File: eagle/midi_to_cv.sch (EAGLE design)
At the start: 49 parts, among them IC1 TL084P, IC2 TL084P, U1 ATMEGA328P_PDIP

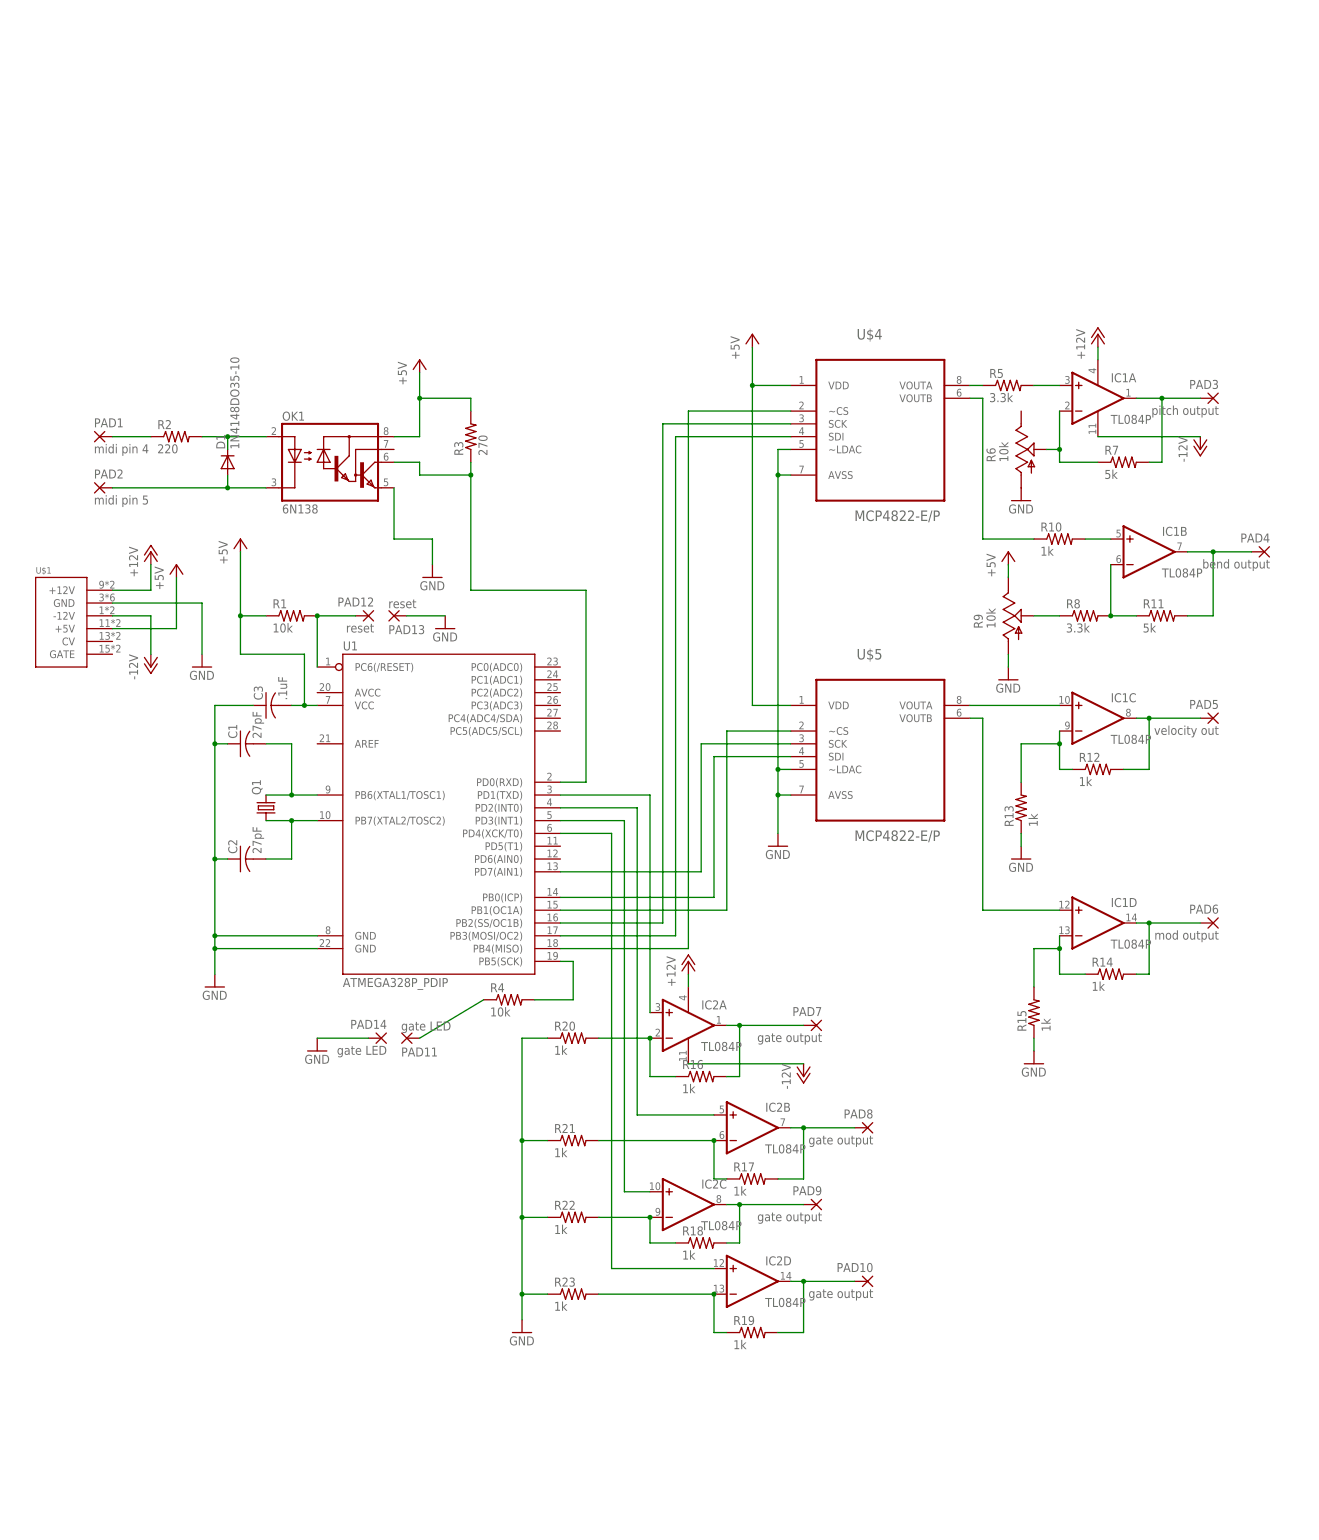
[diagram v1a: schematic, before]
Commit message: this interface is getting sirius
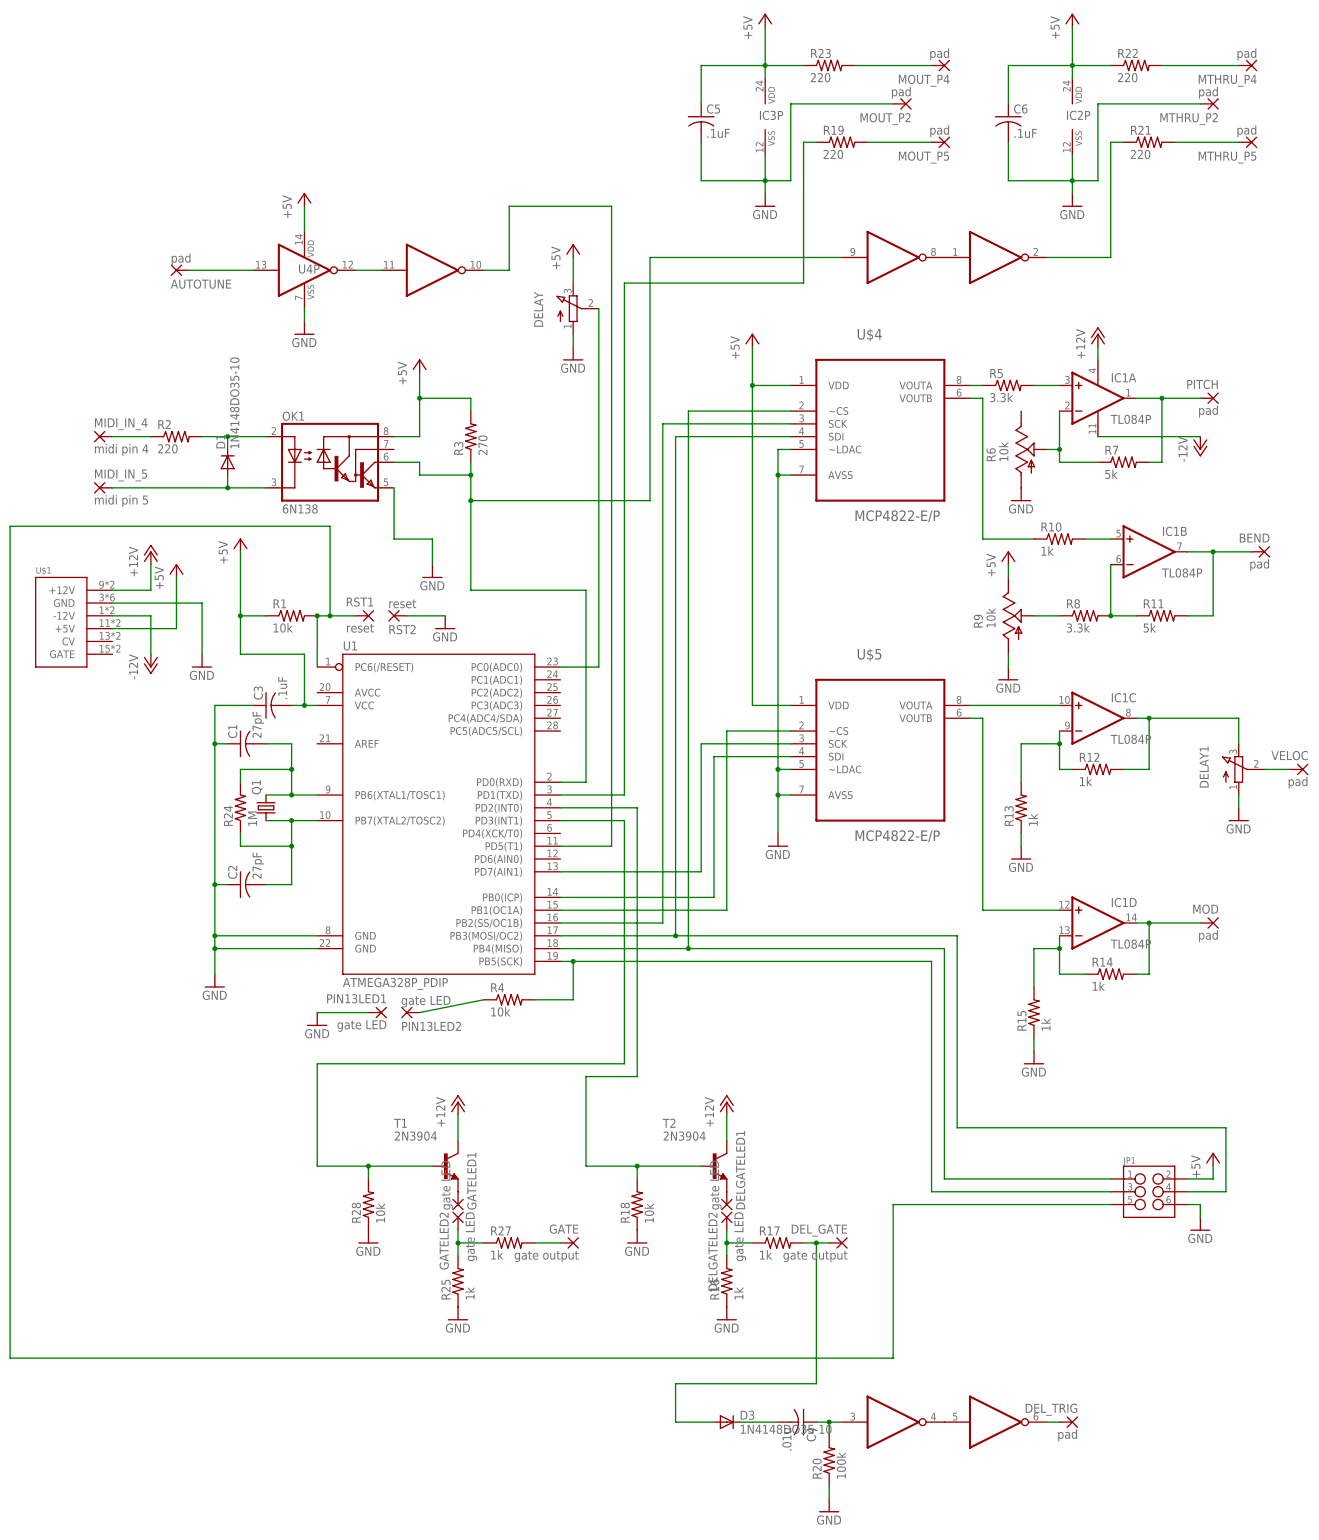
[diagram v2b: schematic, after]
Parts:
- removed PAD10, PAD7, PAD8, PAD9: gate output, wirepad:2,54/0,9
- removed PAD11, PAD14: gate LED, wirepad:2,54/0,9
- removed PAD5: velocity out, wirepad:2,54/0,9
- added AUTOTUNE, DEL_TRIG, MOUT_P2, MOUT_P4, MOUT_P5, MTHRU_P2, MTHRU_P4, MTHRU_P5, VELOC: pad, wirepad:2,54/0,9
- added C4: .01u, rcl:C-US050-024X044
- added C5, C6: .1uF, rcl:C-US025-040X050
- added D3: 1N4148DO35-10, diode:1N4148DO35-10
- added DELAY, DELAY1: (no value), pot:3RP/1610N
- added DELGATELED1, DELGATELED2, GATELED1, GATELED2, PIN13LED1, PIN13LED2: gate LED, wirepad:2,54/0,9
- added DEL_GATE, GATE: gate output, wirepad:2,54/0,9
- added IC3: 4067N, 40xx:4067N
- added JP1: (no value), SparkFun-Connectors:M03X2NO_SILK
- added R24: 1M, rcl:R-US_0207/10
- added R25, R27: 1k, rcl:R-US_0207/10
- added R28: 10k, rcl:R-US_0207/10
- added T1, T2: 2N3904, transistor:2N3904
- added U4: 4584N, TR808clone:4584N
- BEND: value bend output -> pad
- IC2: value TL084P -> 4067N; device linear:TL084P -> 40xx:4067N
- MOD: value mod output -> pad
- PITCH: value pitch output -> pad
- R18: value 1k -> 10k
- R19, R21, R22, R23: value 1k -> 220
- R20: value 1k -> 100k
- renumbered PAD1 to MIDI_IN_4, PAD12 to RST1, PAD13 to RST2, PAD2 to MIDI_IN_5, PAD3 to PITCH, PAD4 to BEND, PAD6 to MOD
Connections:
- removed net N$42: IC2B.-IN, R17.1, R21.2
- new net N$43: JP1.5, R1.2, RST1.P, U1.PC6(/RESET)
- new net N$44: GATE.P, R27.2
- new net N$45: JP1.1, U$4.~CS, U1.PB4(MISO)
- new net N$46: MOUT_P5.P, R19.2
- new net N$47: GATELED2.P, R25.2, R27.1
- new net N$48: C4.2, D3.C
- new net N$49: DEL_TRIG.P, U4C.O
- new net N$50: R21.1, U4A.O
- new net N$51: DELAY1.S, VELOC.P
- new net N$52: MTHRU_P5.P, R21.2
- new net N$54: MTHRU_P4.P, R22.2
- new net N$55: MOUT_P4.P, R23.2
- new net N$57: R19.1, U1.PD1(TXD)
- net +12V: now also T1.C, T2.C; no longer IC2P.V+
- net +5V: now also C5.1, C6.1, DELAY.E, IC2P.VDD, IC3P.VDD, JP1.2, R22.1, R23.1, U4P.VDD
- net -12V: no longer IC2P.V-
- net GND: now also C5.2, C6.2, DELAY.A, DELAY1.A, IC2P.VSS, IC3P.VSS, JP1.6, MOUT_P2.P, MTHRU_P2.P, PIN13LED1.P, R16.1, R18.1, R25.1, R28.1, U4P.VSS; no longer PAD14.P, R21.1, R22.1, R23.1
- net N$1: now also GATELED1.P, T1.E; no longer R1.2, RST1.P, U1.PC6(/RESET)
- net N$10: now also JP1.3
- net N$11: now also PIN13LED2.P; no longer PAD11.P
- net N$19: now also DELAY1.E; no longer PAD5.P
- net N$26: now also JP1.4
- net N$27: now also DELAY.S, U1.PC0(ADC0); no longer U$4.~CS, U1.PB4(MISO)
- net N$30: now also U4D.I
- net N$31: now also DELGATELED1.P, T2.E; no longer IC2A.+IN, U1.PD1(TXD)
- net N$32: now also R18.2, T2.B; no longer IC2B.+IN
- net N$33: now also R28.2, T1.B; no longer IC2C.+IN
- net N$34: now also AUTOTUNE.P, U4F.I; no longer IC2D.+IN, U1.PD4(XCK/T0)
- net N$35: now also D3.A, DEL_GATE.P, R17.2; no longer IC2A.OUT, PAD7.P, R16.2
- net N$36: now also DELGATELED2.P, R16.2, R17.1; no longer IC2B.OUT, PAD8.P, R17.2
- net N$37: now also U4E.I, U4F.O; no longer IC2C.OUT, PAD9.P, R18.2
- net N$38: now also U1.PD5(T1), U4E.O; no longer IC2D.OUT, PAD10.P, R19.2
- net N$39: now also U4A.I, U4D.O; no longer IC2A.-IN, R16.1, R20.2
- net N$4: now also R24.2
- net N$40: now also U4B.O, U4C.I; no longer IC2D.-IN, R19.1, R23.2
- net N$41: now also C4.1, R20.2, U4B.I; no longer IC2C.-IN, R18.1, R22.2
- net N$5: now also R24.1
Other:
- moved on the sheet: C2, R16, R17, R18, R19, R20, R21, R22, R23

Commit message: updated gate circuits and normalled gate and cv to power connector and swapped vel and mod outputs
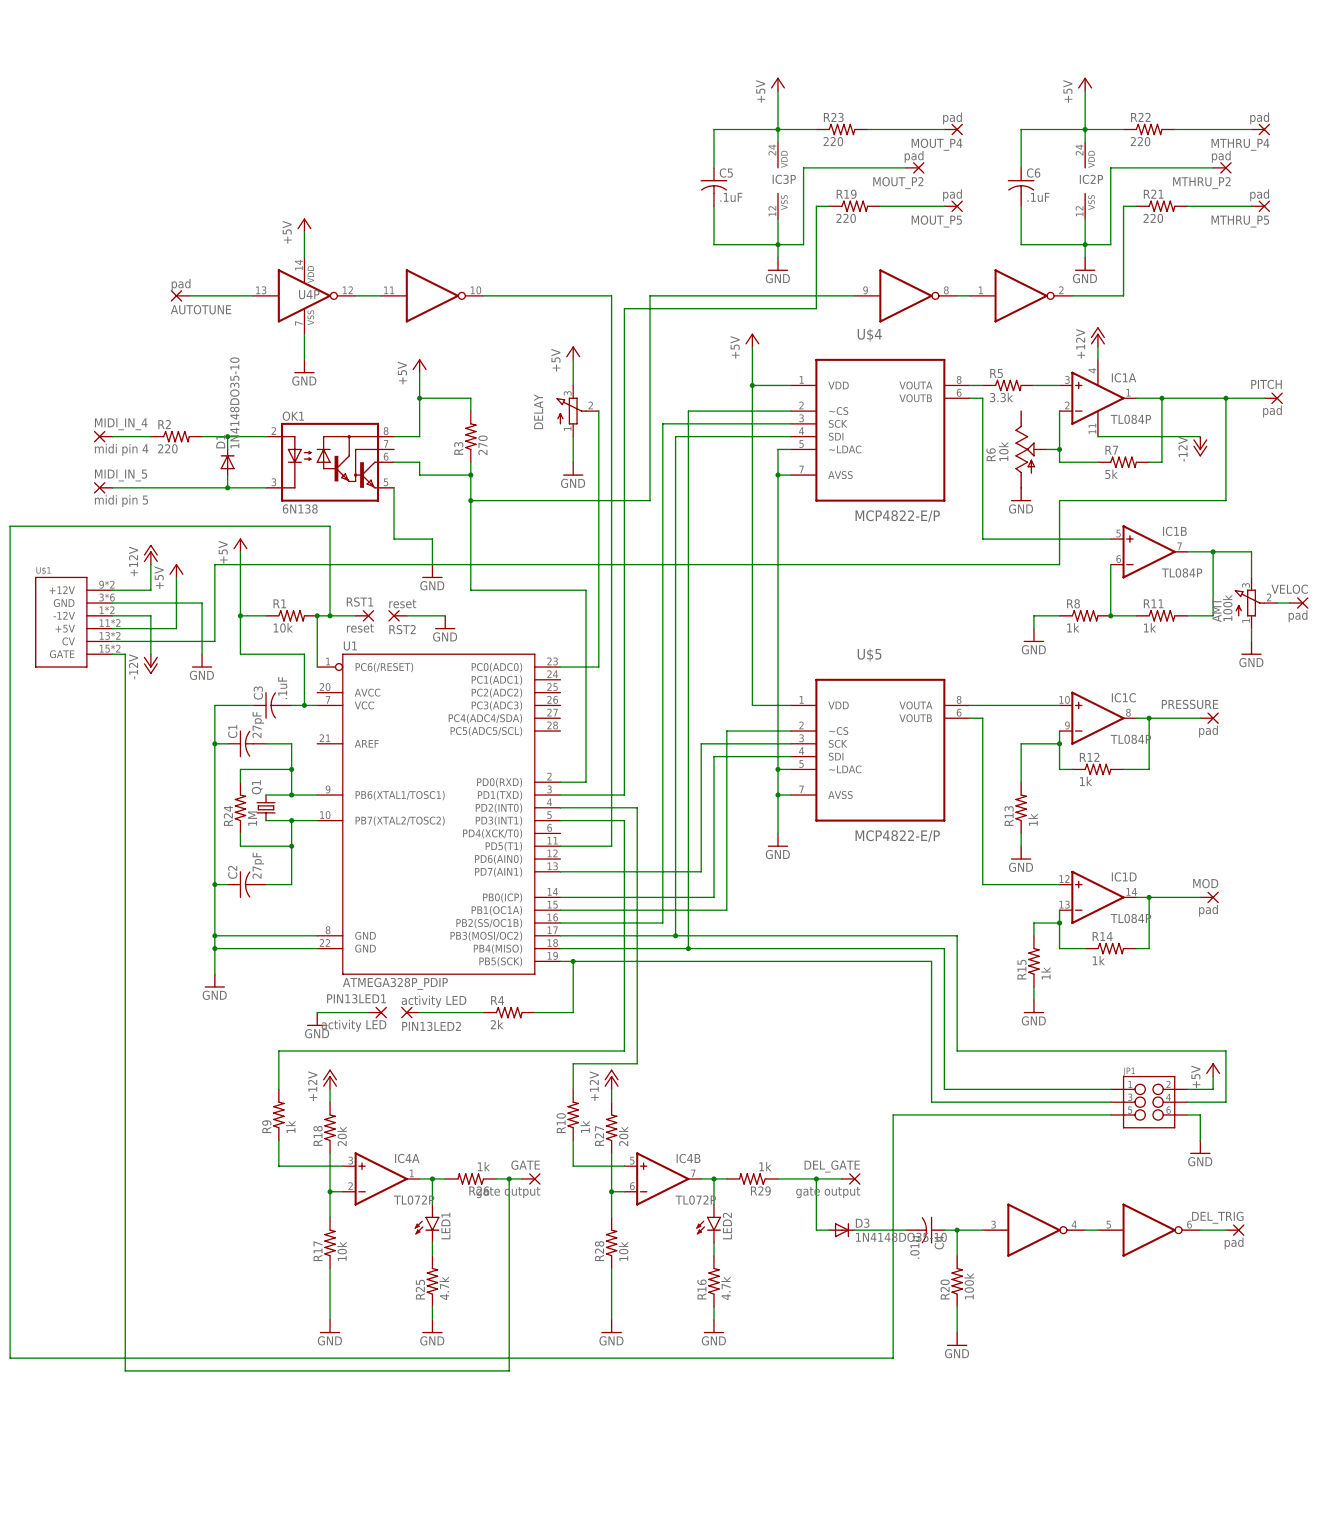
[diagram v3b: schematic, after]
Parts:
- removed BEND: pad, wirepad:2,54/0,9
- removed DELAY1: (no value), pot:3RP/1610N
- removed DELGATELED1, DELGATELED2, GATELED1, GATELED2: gate LED, wirepad:2,54/0,9
- removed T1, T2: 2N3904, transistor:2N3904
- added AMT: 100k, pot:3RP/1610N
- added IC4: TL072P, linear:TL072P
- added LED1, LED2: (no value), SparkFun-LED:LED3MM
- added PRESSURE: pad, wirepad:2,54/0,9
- added R26, R29: 1k, rcl:R-US_0207/10
- PIN13LED1, PIN13LED2: value gate LED -> activity LED
- R11: value 5k -> 1k
- R16, R25: value 1k -> 4.7k
- R17: value 1k -> 10k
- R18: value 10k -> 20k
- R27: value 1k -> 20k
- R4: value 10k -> 2k
- R8: value 3.3k -> 1k
- R9: value 10k -> 1k; device pot:TRIM_US-B64W -> rcl:R-US_0207/10
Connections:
- new net N$42: IC4B.+IN, R10.1
- new net N$53: IC4B.OUT, LED2.A, R29.2
- net +12V: now also R18.2, R27.2; no longer T1.C, T2.C
- net +5V: no longer R9.E
- net GND: now also AMT.A, R17.1, R8.1; no longer DELAY1.A, R18.1, R9.A
- net N$1: now also IC4A.+IN, R9.1; no longer GATELED1.P, T1.E
- net N$14: now also IC1B.+IN; no longer R10.1
- net N$15: now also IC4A.-IN, R17.2, R18.1; no longer IC1B.+IN, R10.2
- net N$16: now also IC4A.OUT, LED1.A, R26.2; no longer R8.1, R9.S
- net N$17: now also AMT.E; no longer BEND.P
- net N$19: now also PRESSURE.P; no longer DELAY1.E
- net N$31: now also GATE.P, R26.1, U$1.GATE; no longer DELGATELED1.P, T2.E
- net N$32: now also R10.2; no longer R18.2, T2.B
- net N$33: now also R9.2; no longer R28.2, T1.B
- net N$35: now also R29.1; no longer R17.2
- net N$36: now also LED2.C; no longer DELGATELED2.P, R17.1
- net N$44: now also IC4B.-IN, R27.1, R28.2; no longer GATE.P, R27.2
- net N$47: now also LED1.C; no longer GATELED2.P, R27.1
- net N$51: now also AMT.S; no longer DELAY1.S
- net N$9: now also U$1.CV
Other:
- moved on the sheet: AUTOTUNE, C4, C5, C6, D3, DELAY, DEL_GATE, DEL_TRIG, GATE, IC1D, IC2P, IC3P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

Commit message: parts basically on board and 072 powered
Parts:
- removed IC2, IC3: 4067N, 40xx:4067N
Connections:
- net +5V: now also IC4P.V+; no longer IC2P.VDD, IC3P.VDD
- net GND: now also IC4P.V-; no longer IC2P.VSS, IC3P.VSS
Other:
- moved on the sheet: U4P
